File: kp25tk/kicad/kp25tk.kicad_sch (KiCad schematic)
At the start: 76 parts, among them J1 Host Connector, J2 Config Header, J3 Power In, J4 Row Select In, J5 Column Out, J6 NMI Out, J7 Reset Out, J8 Switch, SW0 KEY00, SW1 KEY01, SW10 KEY0A, SW11 KEY0B, SW12 KEY0C, SW13 KEY0D, SW14 KEY0E, SW15 KEY0F, SW16 KEY10, SW17 KEY11, SW18 KEY12, SW19 KEY13, SW2 KEY02, SW20 KEY14, SW21 KEY15, SW22 KEY16, SW23 KEY17, SW24 NMI, SW25 RESET, SW27 SWITCH, SW3 KEY03, SW4 KEY04, SW5 KEY05, SW6 KEY06, SW7 KEY07, SW8 KEY08, SW9 KEY09, U1 74LS14

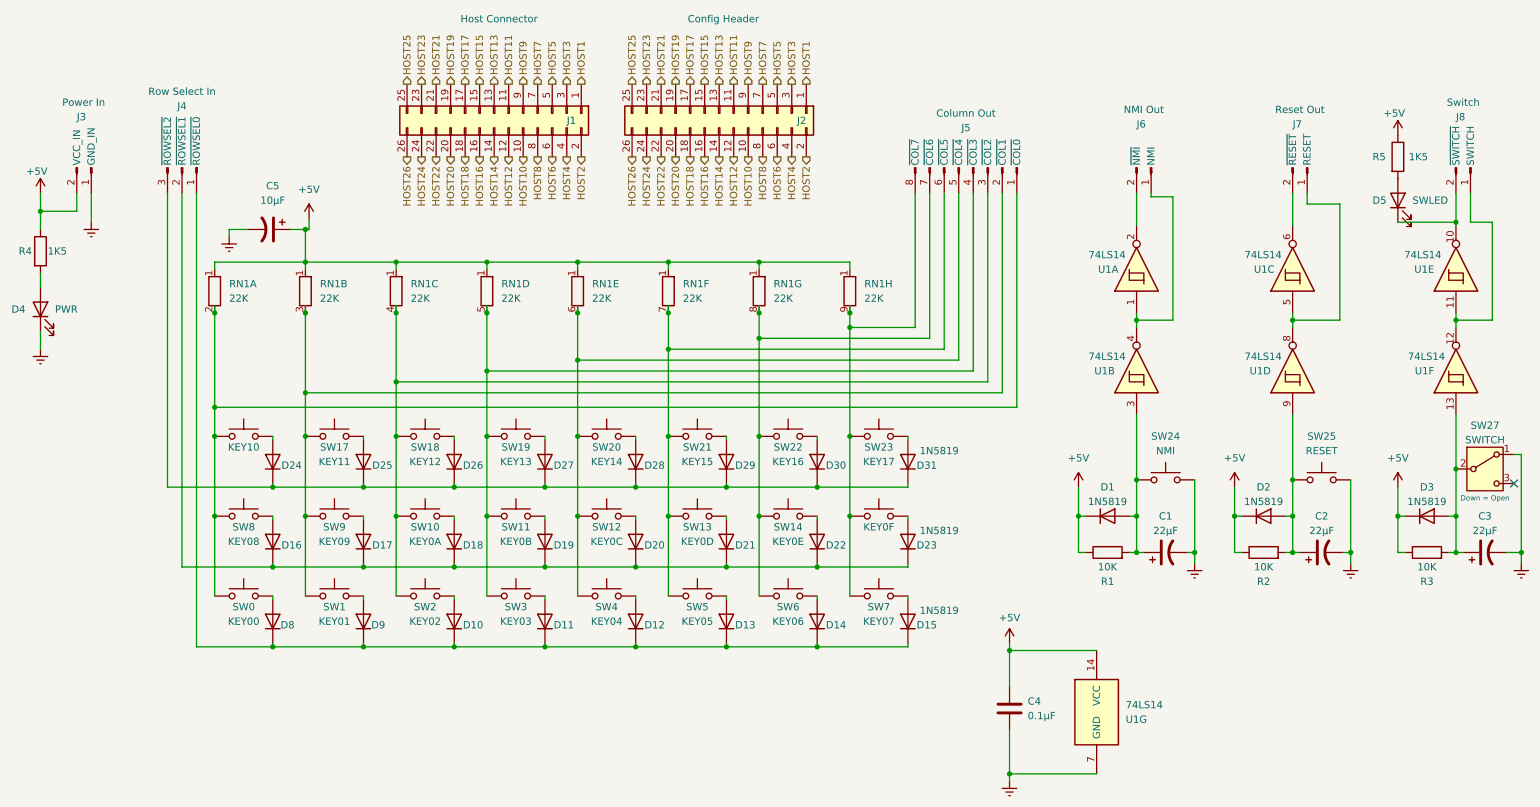
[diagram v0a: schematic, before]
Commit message: kp25tk/: Schematic cleaned up and ready for peer review; more board layout
Board bumped to 0.0.7 to match schematic. Schematic stays there because
it had such minor changes.
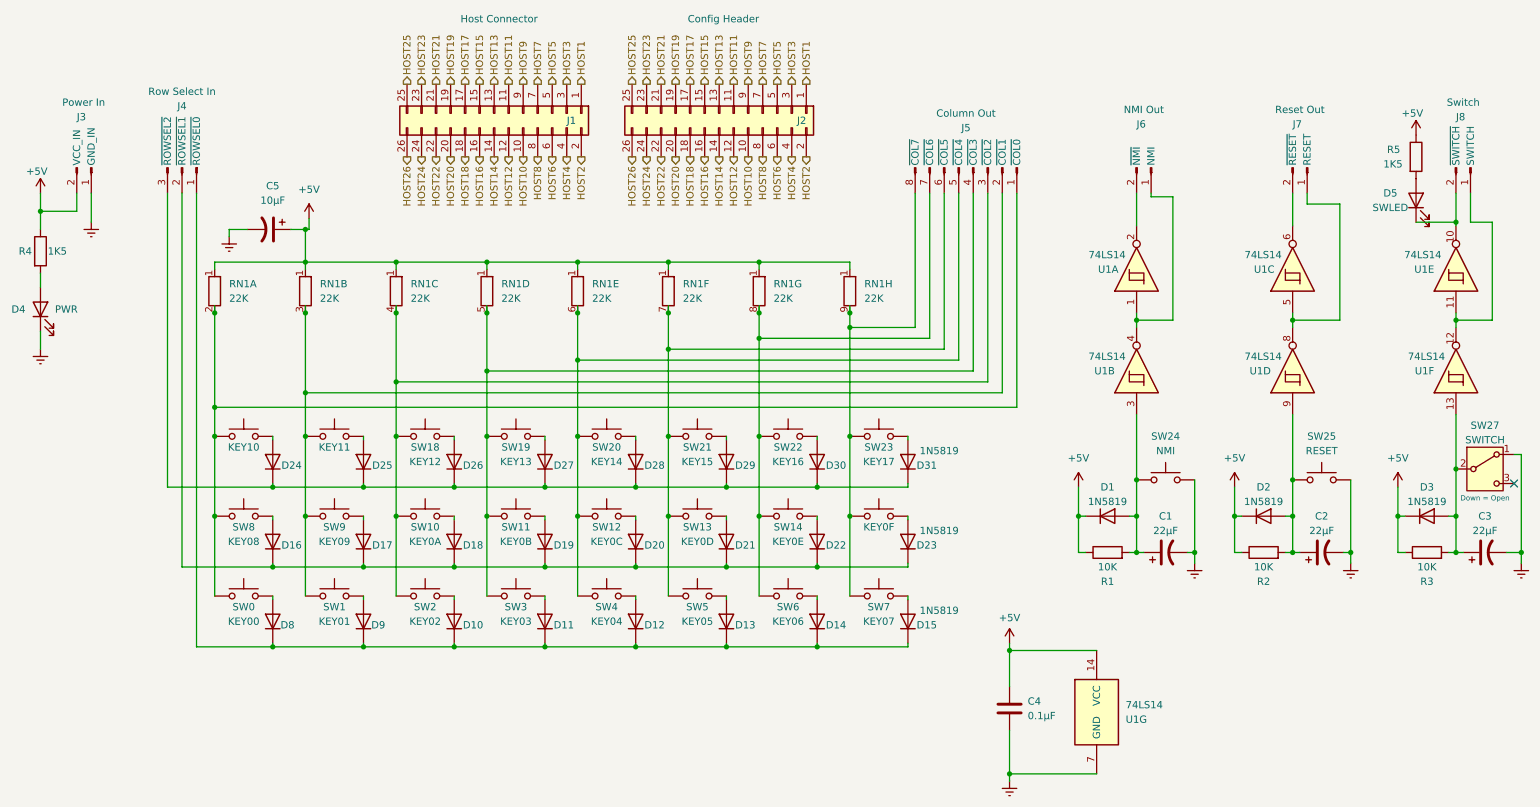
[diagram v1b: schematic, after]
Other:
- moved on the sheet: D5, R5
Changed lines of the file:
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@@
     (stroke (width 0) (type default))
   )
-  (wire (pts (xy 260.35 55.88) (xy 270.51 55.88))
+  (wire (pts (xy 263.525 55.88) (xy 270.51 55.88))
     (stroke (width 0) (type default))
   )
@@
     (in_bom yes) (on_board yes) (dnp no)
     (property "Reference" "SW17" (at 74.295 95.25 0)
-      (effects (font (size 1.27 1.27)))
-    )
-    (property "Value" "KEY11" (at 74.295 97.79 0)
+      (effects (font (size 1.27 1.27)) hide)
+    )
+    (property "Value" "KEY11" (at 74.295 95.25 0)
       (effects (font (size 1.27 1.27)))
     )
@@
     )
   )
-  (symbol (lib_id "Device:R") (at 260.35 44.45 0) (unit 1)
-    (in_bom yes) (on_board yes) (dnp no)
-    (property "Reference" "R5" (at 255.905 44.45 0)
-      (effects (font (size 1.27 1.27)) (justify left))
-    )
-    (property "Value" "1K5" (at 262.255 44.45 0)
-      (effects (font (size 1.27 1.27)) (justify left))
-    )
-    (property "Footprint" "Resistor_THT:R_Axial_DIN0207_L6.3mm_D2.5mm_P10.16mm_Horizontal" (at 258.572 44.45 90)
-      (effects (font (size 1.27 1.27)) hide)
-    )
-    (property "Datasheet" "~" (at 260.35 44.45 0)
+  (symbol (lib_id "Device:R") (at 263.525 44.45 0) (unit 1)
+    (in_bom yes) (on_board yes) (dnp no)
+    (property "Reference" "R5" (at 258.445 43.18 0)
+      (effects (font (size 1.27 1.27)) (justify left))
+    )
+    (property "Value" "1K5" (at 257.81 45.72 0)
+      (effects (font (size 1.27 1.27)) (justify left))
+    )
+    (property "Footprint" "Resistor_THT:R_Axial_DIN0207_L6.3mm_D2.5mm_P10.16mm_Horizontal" (at 261.747 44.45 90)
+      (effects (font (size 1.27 1.27)) hide)
+    )
+    (property "Datasheet" "~" (at 263.525 44.45 0)
       (effects (font (size 1.27 1.27)) hide)
     )
@@
     )
   )
-  (symbol (lib_id "power:+5V") (at 260.35 40.64 0) (unit 1)
-    (in_bom yes) (on_board yes) (dnp no)
-    (property "Reference" "#PWR014" (at 260.35 44.45 0)
-      (effects (font (size 1.27 1.27)) hide)
-    )
-    (property "Value" "+5V" (at 259.715 36.83 0)
-      (effects (font (size 1.27 1.27)))
-    )
-    (property "Footprint" "" (at 260.35 40.64 0)
-      (effects (font (size 1.27 1.27)) hide)
-    )
-    (property "Datasheet" "" (at 260.35 40.64 0)
+  (symbol (lib_id "power:+5V") (at 263.525 40.64 0) (unit 1)
+    (in_bom yes) (on_board yes) (dnp no)
+    (property "Reference" "#PWR014" (at 263.525 44.45 0)
+      (effects (font (size 1.27 1.27)) hide)
+    )
+    (property "Value" "+5V" (at 262.89 36.83 0)
+      (effects (font (size 1.27 1.27)))
+    )
+    (property "Footprint" "" (at 263.525 40.64 0)
+      (effects (font (size 1.27 1.27)) hide)
+    )
+    (property "Datasheet" "" (at 263.525 40.64 0)
       (effects (font (size 1.27 1.27)) hide)
     )
@@
     )
   )
-  (symbol (lib_id "Device:LED") (at 260.35 52.07 90) (unit 1)
-    (in_bom yes) (on_board yes) (dnp no)
-    (property "Reference" "D5" (at 255.905 52.07 90)
+  (symbol (lib_id "Device:LED") (at 263.525 52.07 90) (unit 1)
+    (in_bom yes) (on_board yes) (dnp no)
+    (property "Reference" "D5" (at 257.81 50.8 90)
       (effects (font (size 1.27 1.27)) (justify right))
     )
-    (property "Value" "SWLED" (at 262.89 52.07 90)
+    (property "Value" "SWLED" (at 255.905 53.34 90)
       (effects (font (size 1.27 1.27)) (justify right))
     )
-    (property "Footprint" "LED_THT:LED_D3.0mm" (at 260.35 52.07 0)
-      (effects (font (size 1.27 1.27)) hide)
-    )
-    (property "Datasheet" "~" (at 260.35 52.07 0)
-      (effects (font (size 1.27 1.27)) hide)
-    )
+    (property "Footprint" "LED_THT:LED_D3.0mm" (at 263.525 52.07 0)
+      (effects (font (size 1.27 1.27)) hide)
+    )
+    (property "Datasheet" "~" (at 263.525 52.07 0)
+      (effects (font (size 1.27 1.27)) hide)
+    )

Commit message: kp25tk/: Release candidate 1
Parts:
- U1: value 74LS14 -> 74HLS14
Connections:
- net at C3.1, D3.2 (A), R3.2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: now also D5.1 (K)
- net at J8.2 (~{SWITCH}), U1.10: no longer D5.1 (K)
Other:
- moved on the sheet: D1, D2, D3, D5, R5
